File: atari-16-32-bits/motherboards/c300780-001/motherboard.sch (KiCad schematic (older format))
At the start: 0 parts

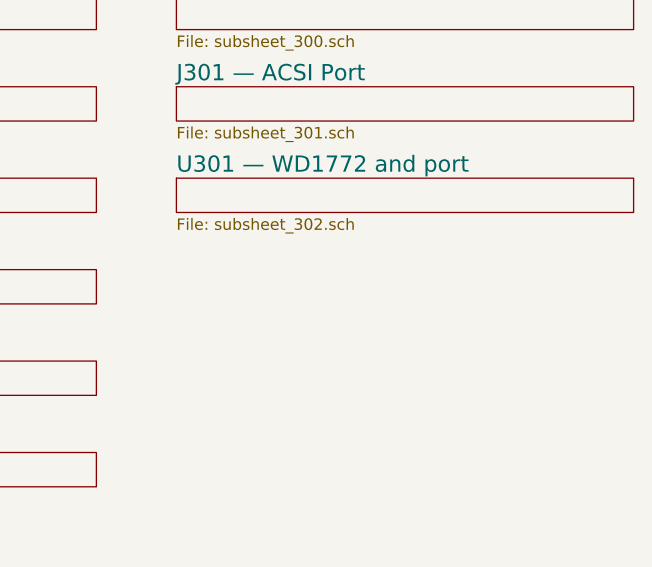
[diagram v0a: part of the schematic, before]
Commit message: subsheet 303 : sclk and clk2
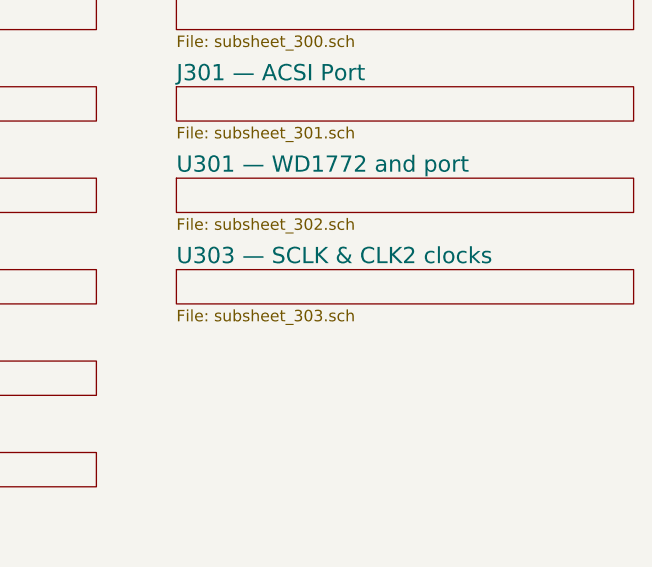
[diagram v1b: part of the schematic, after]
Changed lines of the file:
@@
 $Descr A4 8268 11693 portrait
 encoding utf-8
-Sheet 1 17
+Sheet 1 18
 Title "Converted schematics of Atari STE"
 Date ""
@@
 F1 "subsheet_302.sch" 50
 $EndSheet
+$Sheet
+S 5500 2600 2000 150
+U 60ABB05E
+F0 "U303 — SCLK & CLK2 clocks" 71
+F1 "subsheet_303.sch" 50
+$EndSheet
 $EndSCHEMATC

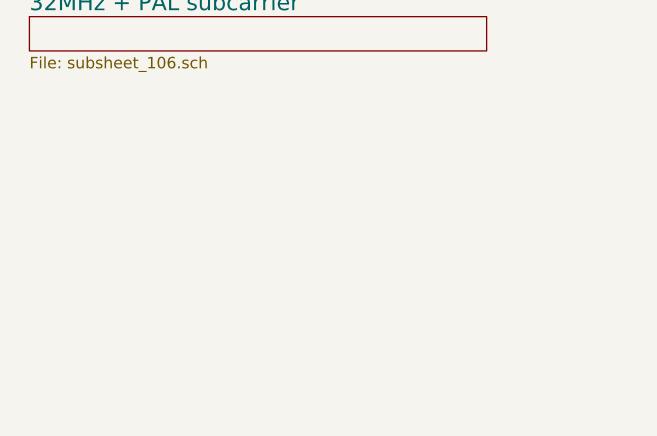
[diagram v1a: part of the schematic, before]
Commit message: started subsheet 400 and 401 : gstmcu and shifter
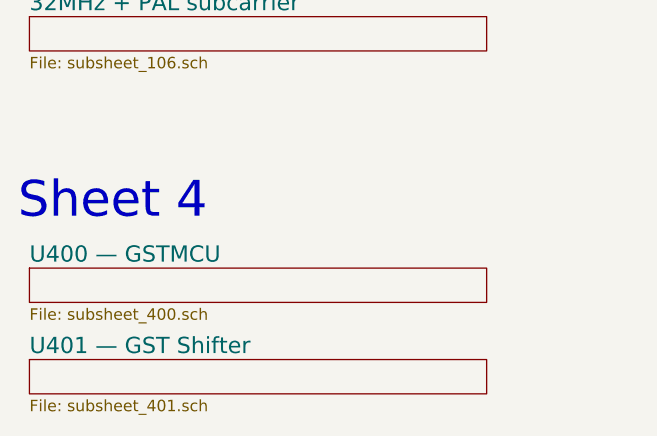
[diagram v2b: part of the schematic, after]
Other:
- note added: "Sheet 4"
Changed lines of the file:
@@
 $Descr A4 8268 11693 portrait
 encoding utf-8
-Sheet 1 18
+Sheet 1 20
 Title "Converted schematics of Atari STE"
 Date ""
@@
 F1 "subsheet_303.sch" 50
 $EndSheet
+Text Notes 750  4700 0    157  ~ 0
+Sheet 4
+$Sheet
+S 800  4900 2000 150
+U 60AD332C
+F0 "U400 — GSTMCU" 71
+F1 "subsheet_400.sch" 50
+$EndSheet
+$Sheet
+S 800  5300 2000 150
+U 60AD33B6
+F0 "U401 — GST Shifter" 71
+F1 "subsheet_401.sch" 50
+$EndSheet
 $EndSCHEMATC

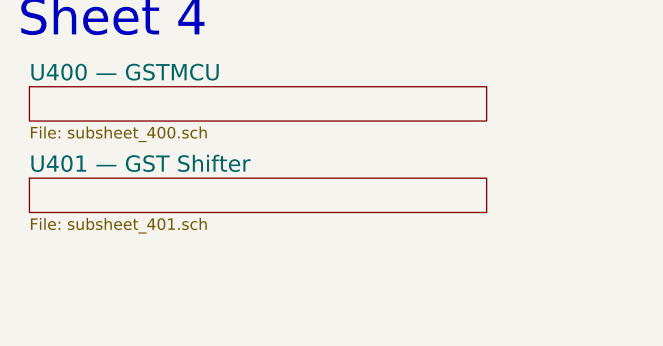
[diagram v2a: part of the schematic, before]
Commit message: wip subsheet 402 : genlock circuitry , remaining R and L annotations
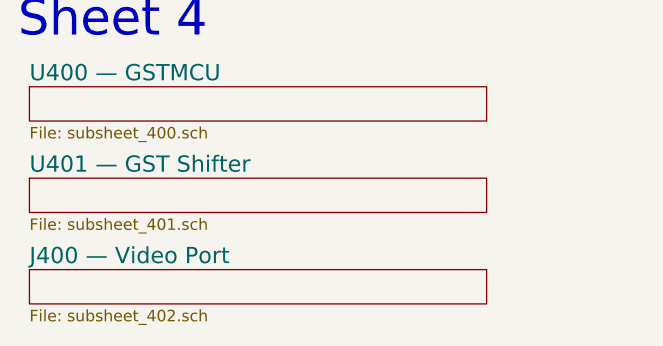
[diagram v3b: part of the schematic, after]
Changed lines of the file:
@@
 $Descr A4 8268 11693 portrait
 encoding utf-8
-Sheet 1 20
+Sheet 1 21
 Title "Converted schematics of Atari STE"
 Date ""
@@
 F1 "subsheet_401.sch" 50
 $EndSheet
+$Sheet
+S 800  5700 2000 150
+U 60B3D9E3
+F0 "J400 — Video Port" 71
+F1 "subsheet_402.sch" 50
+$EndSheet
 $EndSCHEMATC
